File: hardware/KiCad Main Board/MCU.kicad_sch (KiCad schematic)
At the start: 41 parts, among them J1 SWD Debug, J2 USB4105, U1 W25Q128JVS, U7 RP2350B-QFN80, Y1 ABM8-272-T3

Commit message: all GPIO nets connected on schematic
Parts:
- added H1, H2, H3, H4: MountingHole, MountingHole:MountingHole_3.2mm_M3, symbol Mechanical:MountingHole
- added TP10, TP11, TP12, TP13, TP14, TP15, TP16, TP17, TP18, TP19, TP20, TP21, TP22, TP26, TP27, TP28, TP29, TP31, TP32, TP33, TP8, TP9: TestPoint, TestPoint:TestPoint_Pad_D1.0mm, symbol Connector:TestPoint
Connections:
- net 1V1_MCU: now also TP11.1
- net 5V_USB: now also TP12.1
- net AUDIOAMP_I2C_SCL: now also U7.54 (GPIO43_ADC3), TP10.1
- net AUDIOAMP_I2C_SDA: now also U7.53 (GPIO42_ADC2), TP9.1
- net AUDIOAMP_MASTERCLK: now also U7.12 (GPIO13), TP8.1
- net AUDIOAMP_RESET: now also U7.26 (GPIO25)
- net AUDIOAMP_SCL: now also U7.14 (GPIO15), TP28.1
- net AUDIOAMP_SDI: now also U7.13 (GPIO14), TP29.1
- net AUDIOAMP_SDO: now also U7.17 (GPIO17), TP26.1
- net AUDIOAMP_WORDSELECT: now also U7.16 (GPIO16), TP27.1
- net BTN_ENC_A: now also U7.39 (GPIO31)
- net BTN_ENC_B: now also U7.40 (GPIO32)
- net BTN_MTX_0: now also U7.1 (GPIO4)
- net BTN_MTX_1: now also U7.2 (GPIO5)
- net BTN_MTX_2: now also U7.3 (GPIO6)
- net BTN_MTX_3: now also U7.4 (GPIO7)
- net BTN_MTX_4: now also U7.6 (GPIO8)
- net BTN_MTX_5: now also U7.7 (GPIO9)
- net BTN_MTX_A: now also U7.77 (GPIO0)
- net BTN_MTX_B: now also U7.78 (GPIO1)
- net BTN_MTX_C: now also U7.79 (GPIO2)
- net BTN_MTX_D: now also U7.80 (GPIO3)
- net CHGR_STAT: now also U7.25 (GPIO24); no longer U7.55 (GPIO44_ADC4)
- net DISPLAY_BUSY: now also U7.22 (GPIO22)
- net DISPLAY_CS: now also U7.21 (GPIO21)
- net DISPLAY_RESET: now also U7.23 (GPIO23)
- net DISPLAY_SCLK: now also U7.8 (GPIO10), TP13.1
- net DISPLAY_SDI: now also U7.9 (GPIO11), TP14.1
- net FLASH_CS: now also U7.20 (GPIO20)
- net FLASH_SDO: now also U7.11 (GPIO12), TP15.1
- net GND: now also TP31.1
- net HEADSET_CONN: now also U7.55 (GPIO44_ADC4); no longer U7.54 (GPIO43_ADC3)
- net HEADSET_PTT: now also U7.52 (GPIO41_ADC1)
- net LED_STATUS: now also U7.28 (GPIO27)
- net MIC_SCL: now also U7.36 (GPIO28), TP16.1
- net MIC_SDO: now also U7.37 (GPIO29), TP18.1
- net MIC_WORDSELECT: now also U7.38 (GPIO30), TP17.1
- net RF_GPIO0: now also U7.44 (GPIO35)
- net RF_GPIO1: now also U7.43 (GPIO34)
- net RF_GPIO2: now also U7.42 (GPIO33)
- net RF_GPIO3: now also U7.49 (GPIO40_ADC0)
- net RF_SCLK: now also U7.47 (GPIO38), TP21.1
- net RF_SDI: now also U7.48 (GPIO39), TP22.1
- net RF_SDO: now also U7.45 (GPIO36), TP19.1
- net RF_SEL: now also U7.46 (GPIO37), TP20.1
- net SD_CARD_DETECT: now also U7.19 (GPIO19)
- net SD_CS: now also U7.18 (GPIO18)
- net at R50.2: now also U7.27 (GPIO26)
- net at J2.A6 (D+), J2.B6 (D+), R4.2: now also TP32.1
- net at J2.A7 (D-), J2.B7 (D-), R5.2: now also TP33.1
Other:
- moved on the sheet: R50

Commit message: did all the things
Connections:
- net GND: now also R8.2; no longer R8.1
- net at J2.A5 (CC1): now also R8.1; no longer R8.2
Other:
- moved on the sheet: R8
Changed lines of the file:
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@@
 	(symbol
 		(lib_id "Device:R")
-		(at 241.3 35.56 90)
+		(at 241.3 35.56 270)
+		(mirror x)
 		(unit 1)
 		(exclude_from_sim no)
@@
 		(dnp no)
 		(property "Reference" "R8"
-			(at 239.776 33.528 90)
+			(at 242.824 33.528 90)
 			(effects
 				(font
@@
 		)
 		(property "Value" "5k1"
-			(at 243.332 33.528 90)
+			(at 239.268 33.528 90)
 			(effects
 				(font

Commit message: routing PCB
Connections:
- net USB_DP: now reaches R4.1, U7.67 (USB_DP)
- net USB_DN: now reaches R5.1, U7.66 (USB_DM)
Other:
- moved on the sheet: R4, R5
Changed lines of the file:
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@@
 	)
 	(junction
+		(at 157.48 45.72)
+		(diameter 0)
+		(color 0 0 0 0)
+	)
+	(junction
 		(at 30.48 102.87)
 		(diameter 0)
@@
 	)
 	(junction
+		(at 157.48 43.18)
+		(diameter 0)
+		(color 0 0 0 0)
+	)
+	(junction
 		(at 88.9 33.02)
 		(diameter 0)
@@
 	(wire
 		(pts
+			(xy 182.88 43.18) (xy 215.9 43.18)
+		)
+		(stroke
+			(width 0)
+			(type default)
+		)
+	)
+	(wire
+		(pts
+			(xy 157.48 40.64) (xy 157.48 43.18)
+		)
+		(stroke
+			(width 0)
+			(type default)
+		)
+	)
+	(wire
+		(pts
 			(xy 132.08 35.56) (xy 132.08 33.02)
 		)
@@
 	(wire
 		(pts
-			(xy 147.32 45.72) (xy 153.67 45.72)
+			(xy 147.32 45.72) (xy 157.48 45.72)
 		)
 		(stroke
@@
 	(wire
 		(pts
+			(xy 157.48 45.72) (xy 157.48 48.26)
+		)
+		(stroke
+			(width 0)
+			(type default)
+		)
+	)
+	(wire
+		(pts
 			(xy 59.69 88.9) (xy 77.47 88.9)
 		)
@@
 	(wire
 		(pts
-			(xy 161.29 43.18) (xy 215.9 43.18)
-		)
-		(stroke
-			(width 0)
-			(type default)
-		)
-	)
-	(wire
-		(pts
 			(xy 213.36 78.74) (xy 210.82 78.74)
 		)
@@
 	(wire
 		(pts
-			(xy 161.29 45.72) (xy 215.9 45.72)
+			(xy 182.88 45.72) (xy 215.9 45.72)
 		)
 		(stroke
@@
 	(wire
 		(pts
+			(xy 157.48 43.18) (xy 175.26 43.18)
+		)
+		(stroke
+			(width 0)
+			(type default)
+		)
+	)
+	(wire
+		(pts
 			(xy 266.7 68.58) (xy 270.51 68.58)
 		)
@@
 	(wire
 		(pts
+			(xy 157.48 45.72) (xy 175.26 45.72)
+		)
+		(stroke
+			(width 0)
+			(type default)
+		)
+	)
+	(wire
+		(pts
 			(xy 72.39 49.53) (xy 72.39 38.1)
 		)
@@
 	(wire
 		(pts
-			(xy 147.32 43.18) (xy 153.67 43.18)
+			(xy 147.32 43.18) (xy 157.48 43.18)
 		)
 		(stroke
@@
 		)
 	)
+	(global_label "USB_DP"
+		(shape bidirectional)
+		(at 157.48 40.64 0)
+		(fields_autoplaced yes)
+		(effects
+			(font
+				(size 1.27 1.27)
+			)
+			(justify left)
+		)
+		(property "Intersheetrefs" "${INTERSHEET_REFS}"
+			(at 168.8941 40.64 0)
+			(effects
+				(font
+					(size 1.27 1.27)
+				)
+				(justify left)
+				(hide yes)
+			)
+		)
+	)
 	(global_label "BTN_ENC_A"
 		(shape input)
@@
 		)
 	)
+	(global_label "USB_DN"
+		(shape bidirectional)
+		(at 157.48 48.26 0)
+		(fields_autoplaced yes)
+		(effects
+			(font
+				(size 1.27 1.27)
+			)
+			(justify left)
+		)
+		(property "Intersheetrefs" "${INTERSHEET_REFS}"
+			(at 168.9546 48.26 0)
+			(effects
+				(font
+					(size 1.27 1.27)
+				)
+				(justify left)
+				(hide yes)
+			)
+		)
+	)
 	(global_label "BTN_MTX_5"
 		(shape input)
@@
 	(symbol
 		(lib_id "Device:R")
-		(at 157.48 43.18 90)
+		(at 179.07 43.18 90)
 		(unit 1)
 		(exclude_from_sim no)
@@
 		(dnp no)
 		(property "Reference" "R4"
-			(at 155.956 41.148 90)
+			(at 177.546 41.148 90)
 			(effects
 				(font
@@
 		)
 		(property "Value" "27"
-			(at 159.512 41.148 90)
+			(at 181.102 41.148 90)
 			(effects
 				(font
@@
 		)
 		(property "Footprint" "Resistor_SMD:R_0603_1608Metric_Pad0.98x0.95mm_HandSolder"
-			(at 157.48 44.958 90)
+			(at 179.07 44.958 90)
 			(effects
 				(font
@@
 		)
 		(property "Datasheet" "~"
-			(at 157.48 43.18 0)
+			(at 179.07 43.18 0)
 			(effects
 				(font
@@
 		)
 		(property "Description" "Resistor"
-			(at 157.48 43.18 0)
+			(at 179.07 43.18 0)
 			(effects
 				(font
@@
 	(symbol
 		(lib_id "Device:R")
-		(at 157.48 45.72 90)
+		(at 179.07 45.72 90)
 		(unit 1)
 		(exclude_from_sim no)
@@
 		(dnp no)
 		(property "Reference" "R5"
-			(at 155.956 48.006 90)
+			(at 177.546 48.006 90)
 			(effects
 				(font
@@
 		)
 		(property "Value" "27"
-			(at 159.512 48.006 90)
+			(at 181.102 48.006 90)
 			(effects
 				(font
@@
 		)
 		(property "Footprint" "Resistor_SMD:R_0603_1608Metric_Pad0.98x0.95mm_HandSolder"
-			(at 157.48 47.498 90)
+			(at 179.07 47.498 90)
 			(effects
 				(font
@@
 		)
 		(property "Datasheet" "~"
-			(at 157.48 45.72 0)
+			(at 179.07 45.72 0)
 			(effects
 				(font
@@
 		)
 		(property "Description" "Resistor"
-			(at 157.48 45.72 0)
+			(at 179.07 45.72 0)
 			(effects
 				(font

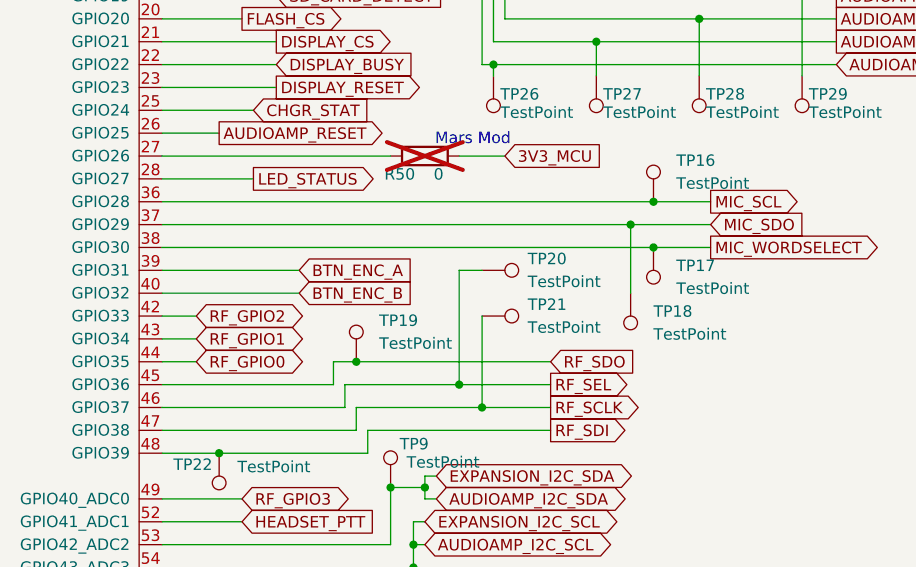
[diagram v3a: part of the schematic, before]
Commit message: finished routing, working on DRC
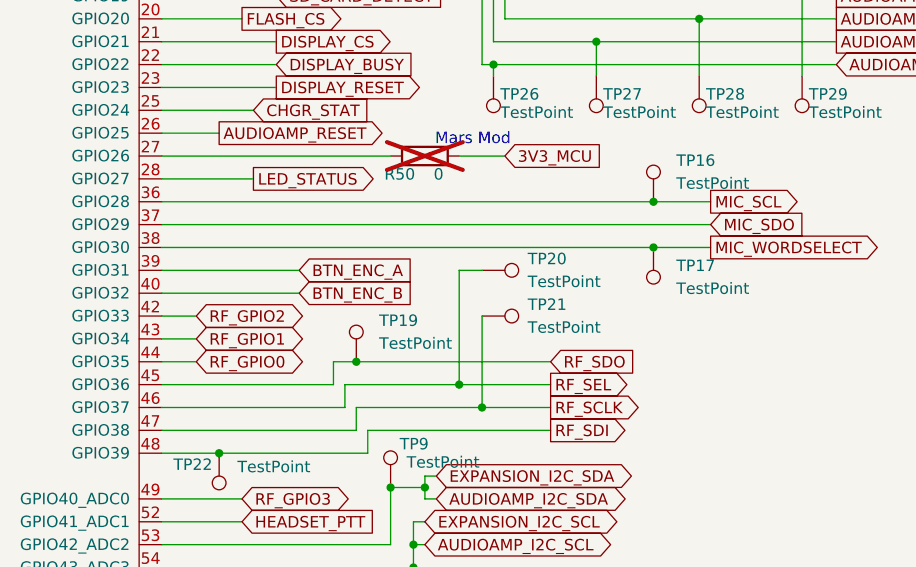
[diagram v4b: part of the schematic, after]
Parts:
- removed TP18: TestPoint, TestPoint:TestPoint_Pad_D1.0mm, symbol Connector:TestPoint
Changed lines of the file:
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@@
 	)
 	(junction
-		(at 199.39 127)
-		(diameter 0)
-		(color 0 0 0 0)
-	)
-	(junction
 		(at 191.77 30.48)
 		(diameter 0)
@@
 	(wire
 		(pts
-			(xy 199.39 134.62) (xy 199.39 127)
-		)
-		(stroke
-			(width 0)
-			(type default)
-		)
-	)
-	(wire
-		(pts
 			(xy 62.23 93.98) (xy 66.04 93.98)
 		)
@@
 	(wire
 		(pts
-			(xy 147.32 127) (xy 199.39 127)
+			(xy 147.32 127) (xy 208.28 127)
 		)
 		(stroke
@@
 	(wire
 		(pts
-			(xy 208.28 127) (xy 199.39 127)
-		)
-		(stroke
-			(width 0)
-			(type default)
-		)
-	)
-	(wire
-		(pts
 			(xy 30.48 82.55) (xy 30.48 86.36)
 		)
@@
 					(unit 1)
 				)
-			)
-		)
-	)
-	(symbol
-		(lib_id "Connector:TestPoint")
-		(at 199.39 134.62 180)
-		(unit 1)
-		(exclude_from_sim no)
-		(in_bom yes)
-		(on_board yes)
-		(dnp no)
-		(fields_autoplaced yes)
-		(property "Reference" "TP18"
-			(at 201.93 136.6519 0)
-			(effects
-				(font
-					(size 1.27 1.27)
-				)
-				(justify right)
-			)
-		)
-		(property "Value" "TestPoint"
-			(at 201.93 139.1919 0)
-			(effects
-				(font
-					(size 1.27 1.27)
-				)
-				(justify right)
-			)
-		)
-		(property "Footprint" "TestPoint:TestPoint_Pad_D1.0mm"
-			(at 194.31 134.62 0)
-			(effects
-				(font
-					(size 1.27 1.27)
-				)
-				(hide yes)
-			)
-		)
-		(property "Datasheet" "~"
-			(at 194.31 134.62 0)
-			(effects
-				(font
-					(size 1.27 1.27)
-				)
-				(hide yes)
-			)
-		)
-		(property "Description" "test point"
-			(at 199.39 134.62 0)
-			(effects
-				(font
-					(size 1.27 1.27)
-				)
-				(hide yes)
-			)
-		)
-		(pin "1"
-		)
-		(instances
-			(project "OSS Radio Hardware Design"
-				(path "/fd5c68a7-f5d0-4135-a258-bde3ebf63307/e0ca9277-1532-4a93-8da4-fd2786b01953"
-					(reference "TP18")
-					(unit 1)
-				)

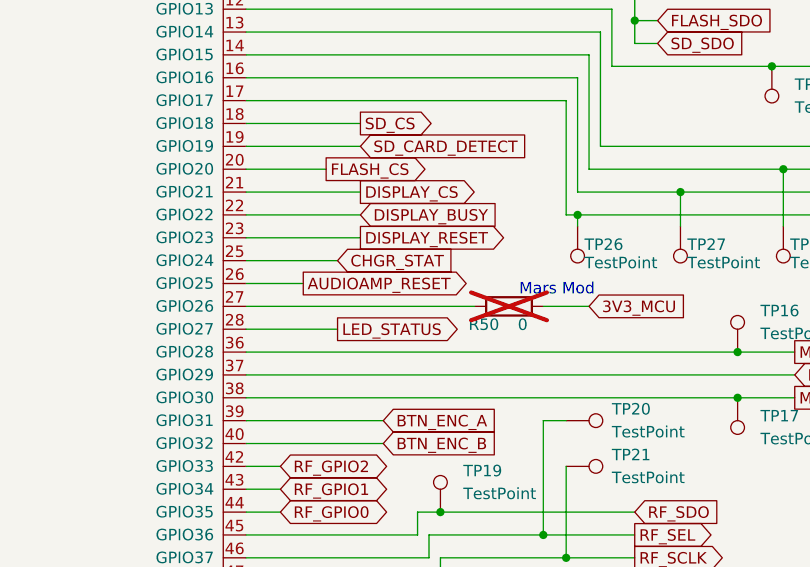
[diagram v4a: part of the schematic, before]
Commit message: made audio amp power swichable
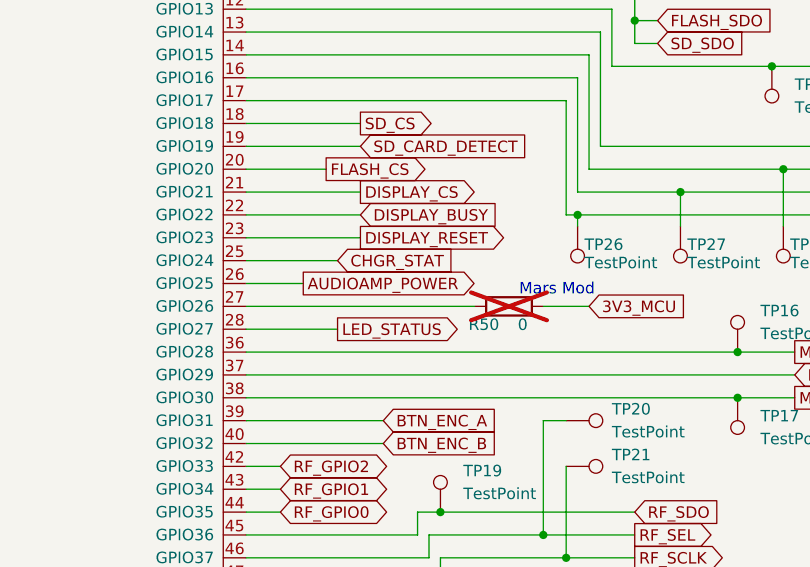
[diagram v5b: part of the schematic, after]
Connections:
- net AUDIOAMP_RESET renamed AUDIOAMP_POWER
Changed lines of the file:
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@@
 		)
 	)
-	(global_label "AUDIOAMP_RESET"
+	(global_label "AUDIOAMP_POWER"
 		(shape output)
 		(at 153.67 116.84 0)
@@
 		)
 		(property "Intersheetrefs" "${INTERSHEET_REFS}"
-			(at 172.8023 116.84 0)
+			(at 173.5281 116.84 0)
 			(effects
 				(font

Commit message: added some notes for RF amp
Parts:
- H1, H2, H3, H4: footprint MountingHole:MountingHole_3.2mm_M3 -> MountingHole:MountingHole_2.2mm_M2
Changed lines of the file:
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@@
 			)
 		)
-		(property "Footprint" "MountingHole:MountingHole_3.2mm_M3"
+		(property "Footprint" "MountingHole:MountingHole_2.2mm_M2"
 			(at 24.13 181.61 0)
 			(effects
@@
 			)
 		)
-		(property "Footprint" "MountingHole:MountingHole_3.2mm_M3"
+		(property "Footprint" "MountingHole:MountingHole_2.2mm_M2"
 			(at 24.13 176.53 0)
 			(effects
@@
 			)
 		)
-		(property "Footprint" "MountingHole:MountingHole_3.2mm_M3"
+		(property "Footprint" "MountingHole:MountingHole_2.2mm_M2"
 			(at 24.13 186.69 0)
 			(effects
@@
 			)
 		)
-		(property "Footprint" "MountingHole:MountingHole_3.2mm_M3"
+		(property "Footprint" "MountingHole:MountingHole_2.2mm_M2"
 			(at 24.13 171.45 0)
 			(effects

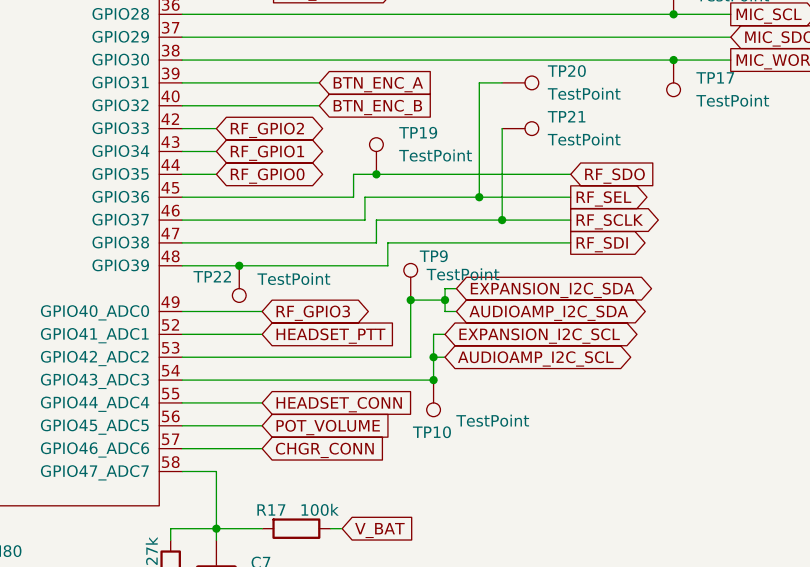
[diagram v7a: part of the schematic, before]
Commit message: changing charging circuitry because the current regulater is linear
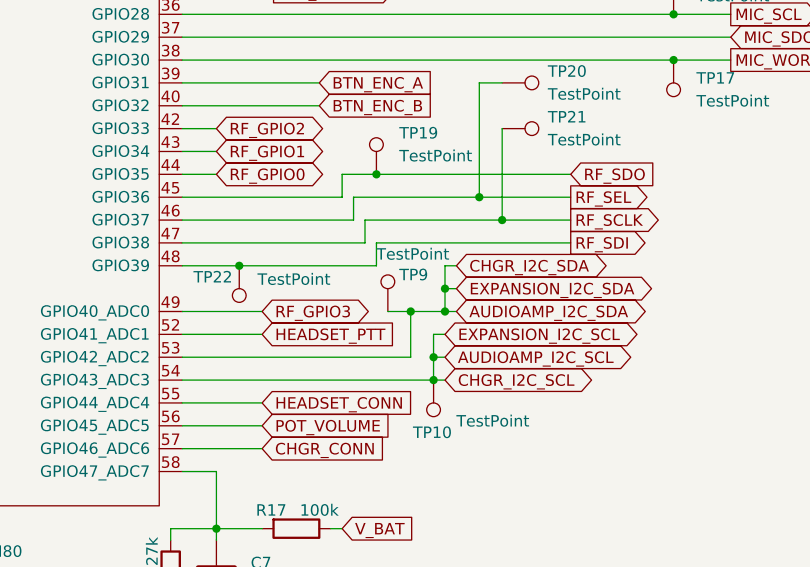
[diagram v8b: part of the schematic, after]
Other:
- moved on the sheet: TP9
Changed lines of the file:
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@@
 	)
 	(junction
-		(at 172.72 156.21)
-		(diameter 0)
-		(color 0 0 0 0)
-	)
-	(junction
 		(at 210.82 81.28)
 		(diameter 0)
@@
 	)
 	(junction
-		(at 176.53 156.21)
-		(diameter 0)
-		(color 0 0 0 0)
-	)
-	(junction
 		(at 175.26 162.56)
 		(diameter 0)
@@
 	)
 	(junction
+		(at 176.53 154.94)
+		(diameter 0)
+		(color 0 0 0 0)
+	)
+	(junction
 		(at 215.9 45.72)
 		(diameter 0)
@@
 	)
 	(junction
+		(at 172.72 157.48)
+		(diameter 0)
+		(color 0 0 0 0)
+	)
+	(junction
 		(at 247.65 48.26)
 		(diameter 0)
@@
 	)
 	(junction
+		(at 176.53 157.48)
+		(diameter 0)
+		(color 0 0 0 0)
+	)
+	(junction
 		(at 212.09 22.86)
 		(diameter 0)
@@
 	(wire
 		(pts
-			(xy 166.37 144.78) (xy 147.32 144.78)
+			(xy 165.1 144.78) (xy 147.32 144.78)
 		)
 		(stroke
@@
 	(wire
 		(pts
-			(xy 168.91 147.32) (xy 182.88 147.32)
+			(xy 167.64 147.32) (xy 182.88 147.32)
 		)
 		(stroke
@@
 	(wire
 		(pts
-			(xy 170.18 149.86) (xy 170.18 152.4)
+			(xy 168.91 149.86) (xy 168.91 152.4)
 		)
 		(stroke
@@
 	(wire
 		(pts
+			(xy 176.53 152.4) (xy 176.53 154.94)
+		)
+		(stroke
+			(width 0)
+			(type default)
+		)
+	)
+	(wire
+		(pts
 			(xy 59.69 88.9) (xy 77.47 88.9)
 		)
@@
 	(wire
 		(pts
+			(xy 177.8 152.4) (xy 176.53 152.4)
+		)
+		(stroke
+			(width 0)
+			(type default)
+		)
+	)
+	(wire
+		(pts
 			(xy 185.42 104.14) (xy 207.01 104.14)
 		)
@@
 	(wire
 		(pts
-			(xy 166.37 142.24) (xy 166.37 144.78)
+			(xy 165.1 142.24) (xy 165.1 144.78)
 		)
 		(stroke
@@
 	(wire
 		(pts
-			(xy 170.18 152.4) (xy 153.67 152.4)
+			(xy 168.91 152.4) (xy 153.67 152.4)
 		)
 		(stroke
@@
 	(wire
 		(pts
-			(xy 167.64 147.32) (xy 147.32 147.32)
+			(xy 166.37 147.32) (xy 147.32 147.32)
 		)
 		(stroke
@@
 	(wire
 		(pts
+			(xy 176.53 165.1) (xy 175.26 165.1)
+		)
+		(stroke
+			(width 0)
+			(type default)
+		)
+	)
+	(wire
+		(pts
 			(xy 59.69 88.9) (xy 59.69 97.79)
 		)
@@
 	(wire
 		(pts
-			(xy 176.53 156.21) (xy 176.53 157.48)
+			(xy 176.53 154.94) (xy 176.53 157.48)
 		)
 		(stroke
@@
 	(wire
 		(pts
-			(xy 172.72 162.56) (xy 172.72 156.21)
+			(xy 172.72 162.56) (xy 172.72 157.48)
 		)
 		(stroke
@@
 	(wire
 		(pts
-			(xy 168.91 147.32) (xy 168.91 149.86)
+			(xy 167.64 147.32) (xy 167.64 149.86)
 		)
 		(stroke
@@
 	(wire
 		(pts
-			(xy 172.72 156.21) (xy 176.53 156.21)
+			(xy 172.72 157.48) (xy 176.53 157.48)
 		)
 		(stroke
@@
 	(wire
 		(pts
+			(xy 170.18 157.48) (xy 172.72 157.48)
+		)
+		(stroke
+			(width 0)
+			(type default)
+		)
+	)
+	(wire
+		(pts
 			(xy 187.96 86.36) (xy 147.32 86.36)
 		)
@@
 	(wire
 		(pts
-			(xy 167.64 144.78) (xy 180.34 144.78)
+			(xy 166.37 144.78) (xy 180.34 144.78)
 		)
 		(stroke
@@
 	(wire
 		(pts
-			(xy 168.91 149.86) (xy 147.32 149.86)
+			(xy 167.64 149.86) (xy 147.32 149.86)
 		)
 		(stroke
@@
 	(wire
 		(pts
-			(xy 170.18 149.86) (xy 190.5 149.86)
+			(xy 168.91 149.86) (xy 190.5 149.86)
 		)
 		(stroke
@@
 	(wire
 		(pts
-			(xy 166.37 142.24) (xy 168.91 142.24)
+			(xy 165.1 142.24) (xy 168.91 142.24)
 		)
 		(stroke
@@
 	(wire
 		(pts
-			(xy 176.53 154.94) (xy 176.53 156.21)
-		)
-		(stroke
-			(width 0)
-			(type default)
-		)
-	)
-	(wire
-		(pts
 			(xy 120.65 22.86) (xy 116.84 22.86)
 		)
@@
 	(wire
 		(pts
-			(xy 167.64 144.78) (xy 167.64 147.32)
+			(xy 166.37 144.78) (xy 166.37 147.32)
 		)
 		(stroke
@@
 				)
 			)
-			(table_cell "Audio IC, Expansion"
+			(table_cell "Audio IC, Expansion, Battery Charger"
 				(exclude_from_sim no)
 				(at 218.44 151.13 0)
@@
 		)
 	)
+	(global_label "CHGR_I2C_SDA"
+		(shape bidirectional)
+		(at 177.8 152.4 0)
+		(fields_autoplaced yes)
+		(effects
+			(font
+				(size 1.27 1.27)
+			)
+			(justify left)
+		)
+		(property "Intersheetrefs" "${INTERSHEET_REFS}"
+			(at 195.6246 152.4 0)
+			(effects
+				(font
+					(size 1.27 1.27)
+				)
+				(justify left)
+				(hide yes)
+			)
+		)
+	)
 	(global_label "BTN_MTX_B"
 		(shape output)
@@
 		)
 	)
+	(global_label "CHGR_I2C_SCL"
+		(shape bidirectional)
+		(at 176.53 165.1 0)
+		(fields_autoplaced yes)
+		(effects
+			(font
+				(size 1.27 1.27)
+			)
+			(justify left)
+		)
+		(property "Intersheetrefs" "${INTERSHEET_REFS}"
+			(at 194.2941 165.1 0)
+			(effects
+				(font
+					(size 1.27 1.27)
+				)
+				(justify left)
+				(hide yes)
+			)
+		)
+	)
 	(global_label "AUDIOAMP_SCL"
 		(shape output)
@@
 	(symbol
 		(lib_id "Connector:TestPoint")
-		(at 172.72 156.21 0)
+		(at 170.18 157.48 0)
 		(unit 1)
 		(exclude_from_sim no)
@@
 		(dnp no)
 		(property "Reference" "TP9"
-			(at 173.736 151.384 0)
+			(at 171.45 153.416 0)
 			(effects
 				(font
@@
 		)
 		(property "Value" "TestPoint"
-			(at 174.498 153.416 0)
+			(at 168.91 151.13 0)
 			(effects
 				(font
@@
 		)
 		(property "Footprint" "TestPoint:TestPoint_Pad_D1.0mm"
-			(at 177.8 156.21 0)
+			(at 175.26 157.48 0)
 			(effects
 				(font
@@
 		)
 		(property "Datasheet" "~"
-			(at 177.8 156.21 0)
+			(at 175.26 157.48 0)
 			(effects
 				(font
@@
 		)
 		(property "Description" "test point"
-			(at 172.72 156.21 0)
+			(at 170.18 157.48 0)
 			(effects
 				(font
